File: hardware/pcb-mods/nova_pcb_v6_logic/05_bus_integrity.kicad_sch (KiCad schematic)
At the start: 2 parts

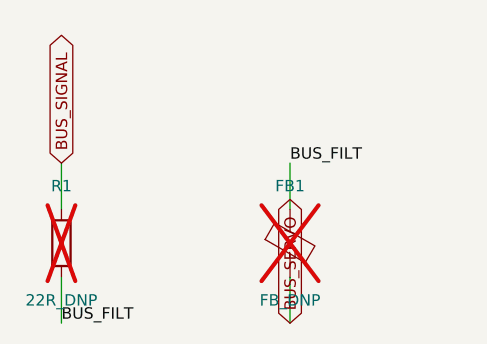
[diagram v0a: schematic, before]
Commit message: fix(logic): un-DNP R1 (22R) + FB1 (ferrite) — series bus parts must be populated
Bug found in 2026-06-13 review: BUS_SIGNAL(74HC125 out)->R1->FB1->BUS_SERVO
runs through both parts IN SERIES with no bypass. DNP = open bus.
Original §5 intent (optional tuning footprints, populate-if-noisy) was
sound but they're load-bearing in the only path. Populate by default:
R1=22R (source termination, reduces ringing — good regardless),
FB1=ferrite (common-mode rejection). Tune values later if needed,
never depopulate. ERC: no new violations (18 pre-existing logic-board
in-progress items remain).

Co-Authored-By: Claude Fable 5 <noreply@anthropic.com>
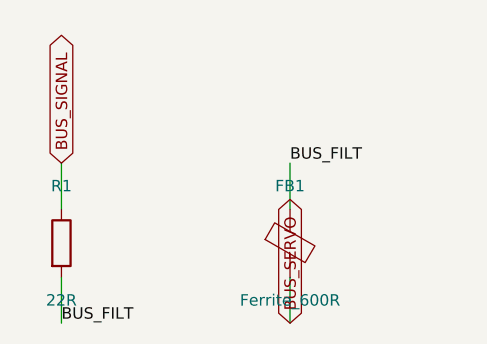
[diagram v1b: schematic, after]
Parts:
- FB1: value FB_DNP -> Ferrite_600R; now fitted
- R1: value 22R_DNP -> 22R; now fitted
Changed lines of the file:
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@@
 		(in_bom yes)
 		(on_board yes)
-		(dnp yes)
+		(dnp no)
 		(property "Reference" "FB1"
 			(at 101.6 57.15 0)
@@
 			)
 		)
-		(property "Value" "FB_DNP"
+		(property "Value" "Ferrite_600R"
 			(at 101.6 69.85 0)
 			(effects
@@
 		(in_bom yes)
 		(on_board yes)
-		(dnp yes)
+		(dnp no)
 		(property "Reference" "R1"
 			(at 76.2 57.15 0)
@@
 			)
 		)
-		(property "Value" "22R_DNP"
+		(property "Value" "22R"
 			(at 76.2 69.85 0)
 			(effects

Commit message: logic board: U7 -> SN74LVC125A (5V-tolerant) + R7 bus idle pull-up
Full-review findings from the servo-bus level analysis:

U7: 74HC125 -> SN74LVC125A. The 74HC125 at +3V3 is NOT 5V-tolerant
(input abs-max VCC+0.5=3.8V); the STS3215 bus is 5V-TTL, so the servo's
response would over-drive gate2's input (clamp current ~54mA through R1's
22ohm). LVC125A is a drop-in SOIC-14, VCC 3.3V (max 3.6V), 5V-tolerant
inputs, 3.3V outputs (Teensy-safe) -> correct whether bus is 3.3V or 5V.
Value-only change (was stale "74LS125" in sch / "74HC125" in pcb; both
wrong for a 3.3V rail), no reroute. Unified all 5 U7 units + pcb value.

R7 = 10k bus idle pull-up (BUS_SIGNAL -> +3V3). Half-duplex push-pull bus
floats in TX/RX turnaround; R7 holds idle HIGH. Added incrementally
(footprint + 2 hand-routed nets) without disturbing the 154 existing
tracks/pours. Routed pad1->U7.10 (+3V3), pad2 down-and-around below U7 to
the BUS_SIGNAL run (staying clear of the MASTER_A diagonal).

Both boards DRC 0/0. Logic ERC = same known items (no new). Gerbers re-cut.
BOM: order SN74LVC125AD + 10k 0603. Firmware unchanged (hardware-only).

Co-Authored-By: Claude Opus 4.8 <noreply@anthropic.com>
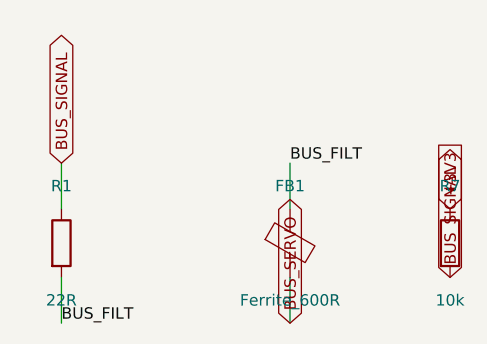
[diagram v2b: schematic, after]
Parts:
- added R7: 10k, Resistor_SMD:R_0603_1608Metric, symbol Device:R
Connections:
- net BUS_SIGNAL: now also R7.2
- new net +3V3: R7.1
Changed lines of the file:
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@@
 		)
+	)
+	(symbol
+		(lib_id "Device:R")
+		(at 119.38 63.5 0)(unit 1)
+		(exclude_from_sim no)(in_bom yes)(on_board yes)(dnp no)
+		(property "Reference" "R7" (at 119.38 57.15 0)(effects (font (size 1.27 1.27))))
+		(property "Value" "10k" (at 119.38 69.85 0)(effects (font (size 1.27 1.27))))
+		(property "Footprint" "Resistor_SMD:R_0603_1608Metric" (at 119.38 63.5 0)(effects (font (size 1.27 1.27))(hide yes)))
+		(property "Datasheet" "~" (at 119.38 63.5 0)(effects (font (size 1.27 1.27))(hide yes)))
+		(property "Description" "" (at 119.38 63.5 0)(effects (font (size 1.27 1.27))))
+		(pin "1")
+		(pin "2")
+		(instances (project "nova_pcb_v6_logic" (path "/f535083b-f621-4317-a378-cf746e7f972b/45d7d740-e2f4-40d0-8d10-022e9099f66d" (reference "R7")(unit 1))))
+	)
+	(global_label "+3V3"
+		(shape input)(at 119.38 59.69 90)
+		(effects (font (size 1.27 1.27))(justify left))
+		(property "Intersheetrefs" "${INTERSHEET_REFS}" (at 119.38 59.69 0)(effects (font (size 1.27 1.27))(hide yes)))
+	)
+	(global_label "BUS_SIGNAL"
+		(shape bidirectional)(at 119.38 67.31 270)
+		(effects (font (size 1.27 1.27))(justify left))
+		(property "Intersheetrefs" "${INTERSHEET_REFS}" (at 119.38 67.31 0)(effects (font (size 1.27 1.27))(hide yes)))
 	)
 	(sheet_instances
